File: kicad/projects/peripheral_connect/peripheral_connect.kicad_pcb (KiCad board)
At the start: 2 copper layers, 203.2 x 97.8 mm, 6 parts, among them J1 peripheral_addr_bus_connector, J2 peripheral_aux_connector, J3 peripheral_membank_connector

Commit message: Rough layout of peripheral connect PCB.
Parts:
- added C1: C, Capacitor_THT:C_Disc_D5.0mm_W2.5mm_P5.00mm, F.Cu at (90.9, 89.4)
- added C2: C, Capacitor_THT:C_Disc_D5.0mm_W2.5mm_P5.00mm, F.Cu at (89.7, 116.6)
- added C3: C, Capacitor_THT:C_Disc_D5.0mm_W2.5mm_P5.00mm, F.Cu at (133.1, 116.3)
- added C4: C, Capacitor_THT:C_Disc_D5.0mm_W2.5mm_P5.00mm, F.Cu at (98.6, 118.1)
- added C5: C, Capacitor_THT:C_Disc_D5.0mm_W2.5mm_P5.00mm, F.Cu at (200.7, 78.7)
- added C6: C, Capacitor_THT:C_Disc_D5.0mm_W2.5mm_P5.00mm, F.Cu at (155.8, 77.7)
- added C7: C, Capacitor_THT:C_Disc_D5.0mm_W2.5mm_P5.00mm, F.Cu at (102.1, 84.3)
- added C8: C, Capacitor_THT:C_Disc_D5.0mm_W2.5mm_P5.00mm, F.Cu at (54.9, 82.3)
- added D1: LED, sixteen-bit-computer:LED_D5.0mm_Horizontal_O3.81mm_Z3.0mm, F.Cu at (251.5, 63.5)
- added D10: LED, sixteen-bit-computer:LED_D5.0mm_Horizontal_O3.81mm_Z3.0mm, F.Cu at (196.6, 63.5)
- added D11: LED, sixteen-bit-computer:LED_D5.0mm_Horizontal_O3.81mm_Z3.0mm, F.Cu at (190.5, 63.5)
- added D12: LED, sixteen-bit-computer:LED_D5.0mm_Horizontal_O3.81mm_Z3.0mm, F.Cu at (184.4, 63.5)
- added D13: LED, sixteen-bit-computer:LED_D5.0mm_Horizontal_O3.81mm_Z3.0mm, F.Cu at (178.3, 63.5)
- added D14: LED, sixteen-bit-computer:LED_D5.0mm_Horizontal_O3.81mm_Z3.0mm, F.Cu at (172.2, 63.5)
- added D15: LED, sixteen-bit-computer:LED_D5.0mm_Horizontal_O3.81mm_Z3.0mm, F.Cu at (166.1, 63.5)
- added D16: LED, sixteen-bit-computer:LED_D5.0mm_Horizontal_O3.81mm_Z3.0mm, F.Cu at (160.0, 63.5)
- added D17: LED, sixteen-bit-computer:LED_D5.0mm_Horizontal_O3.81mm_Z3.0mm, F.Cu at (147.3, 63.5)
- added D18: LED, sixteen-bit-computer:LED_D5.0mm_Horizontal_O3.81mm_Z3.0mm, F.Cu at (141.2, 63.5)
- added D19: LED, sixteen-bit-computer:LED_D5.0mm_Horizontal_O3.81mm_Z3.0mm, F.Cu at (135.1, 63.5)
- added D2: LED, sixteen-bit-computer:LED_D5.0mm_Horizontal_O3.81mm_Z3.0mm, F.Cu at (245.4, 63.5)
- added D20: LED, sixteen-bit-computer:LED_D5.0mm_Horizontal_O3.81mm_Z3.0mm, F.Cu at (129.0, 63.5)
- added D21: LED, sixteen-bit-computer:LED_D5.0mm_Horizontal_O3.81mm_Z3.0mm, F.Cu at (122.9, 63.5)
- added D22: LED, sixteen-bit-computer:LED_D5.0mm_Horizontal_O3.81mm_Z3.0mm, F.Cu at (116.8, 63.5)
- added D23: LED, sixteen-bit-computer:LED_D5.0mm_Horizontal_O3.81mm_Z3.0mm, F.Cu at (110.7, 63.5)
- added D24: LED, sixteen-bit-computer:LED_D5.0mm_Horizontal_O3.81mm_Z3.0mm, F.Cu at (104.6, 63.5)
- added D25: LED, sixteen-bit-computer:LED_D5.0mm_Horizontal_O3.81mm_Z3.0mm, F.Cu at (98.6, 63.5)
- added D26: LED, sixteen-bit-computer:LED_D5.0mm_Horizontal_O3.81mm_Z3.0mm, F.Cu at (92.5, 63.5)
- added D27: LED, sixteen-bit-computer:LED_D5.0mm_Horizontal_O3.81mm_Z3.0mm, F.Cu at (86.4, 63.5)
- added D28: LED, sixteen-bit-computer:LED_D5.0mm_Horizontal_O3.81mm_Z3.0mm, F.Cu at (80.3, 63.5)
- added D29: LED, sixteen-bit-computer:LED_D5.0mm_Horizontal_O3.81mm_Z3.0mm, F.Cu at (74.2, 63.5)
- added D3: LED, sixteen-bit-computer:LED_D5.0mm_Horizontal_O3.81mm_Z3.0mm, F.Cu at (239.3, 63.5)
- added D30: LED, sixteen-bit-computer:LED_D5.0mm_Horizontal_O3.81mm_Z3.0mm, F.Cu at (68.1, 63.5)
- added D31: LED, sixteen-bit-computer:LED_D5.0mm_Horizontal_O3.81mm_Z3.0mm, F.Cu at (62.0, 63.5)
- added D32: LED, sixteen-bit-computer:LED_D5.0mm_Horizontal_O3.81mm_Z3.0mm, F.Cu at (55.9, 63.5)
- added D4: LED, sixteen-bit-computer:LED_D5.0mm_Horizontal_O3.81mm_Z3.0mm, F.Cu at (233.2, 63.5)
- added D5: LED, sixteen-bit-computer:LED_D5.0mm_Horizontal_O3.81mm_Z3.0mm, F.Cu at (227.1, 63.5)
- added D6: LED, sixteen-bit-computer:LED_D5.0mm_Horizontal_O3.81mm_Z3.0mm, F.Cu at (221.0, 63.5)
- added D7: LED, sixteen-bit-computer:LED_D5.0mm_Horizontal_O3.81mm_Z3.0mm, F.Cu at (214.9, 63.5)
- added D8: LED, sixteen-bit-computer:LED_D5.0mm_Horizontal_O3.81mm_Z3.0mm, F.Cu at (208.8, 63.5)
- added D9: LED, sixteen-bit-computer:LED_D5.0mm_Horizontal_O3.81mm_Z3.0mm, F.Cu at (202.7, 63.5)
- added J6: Conn_02x16_Odd_Even, Connector_PinHeader_2.54mm:PinHeader_2x16_P2.54mm_Vertical, F.Cu at (61.0, 91.7)
- added J7: ADDR, Connector_PinHeader_2.54mm:PinHeader_2x17_P2.54mm_Vertical, F.Cu at (203.2, 102.9)
- added J8: DATA, Connector_PinHeader_2.54mm:PinHeader_2x17_P2.54mm_Vertical, F.Cu at (243.8, 121.9)
- added RN1: R_Network08_US, Resistor_THT:R_Array_SIP9, F.Cu at (216.9, 70.6)
- added RN2: R_Network08_US, Resistor_THT:R_Array_SIP9, F.Cu at (170.2, 69.8)
- added RN3: R_Network08_US, Resistor_THT:R_Array_SIP9, F.Cu at (115.3, 69.6)
- added RN4: R_Network08_US, Resistor_THT:R_Array_SIP9, F.Cu at (66.8, 70.1)
- added U1: 74HC138, Package_DIP:DIP-16_W7.62mm_Socket, F.Cu at (150.6, 120.9)
- added U2: 74HC138, Package_DIP:DIP-16_W7.62mm_Socket, F.Cu at (116.1, 122.4)
- added U3: 74HC238, Package_DIP:DIP-16_W7.62mm_Socket, F.Cu at (77.5, 116.8)
- added U4: 74HC245, Package_DIP:DIP-20_W7.62mm_Socket, F.Cu at (210.3, 84.3)
- added U5: 74HC238, Package_DIP:DIP-16_W7.62mm_Socket, F.Cu at (77.5, 89.9)
- added U6: 74HC245, Package_DIP:DIP-20_W7.62mm_Socket, F.Cu at (164.8, 83.3)
- added U7: 74HC245, Package_DIP:DIP-20_W7.62mm_Socket, F.Cu at (109.7, 81.8)
- added U8: 74HC245, Package_DIP:DIP-20_W7.62mm_Socket, F.Cu at (62.2, 83.1)
- moved C99 33.2 mm to (29.3, 145.5)
- moved C97 27.7 mm to (37.7, 42.7)
- moved C98 26.8 mm to (266.0, 46.0)
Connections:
- J2 pad 10: unconnected-(J2-RFM-Pad10) -> /RFM
- J2 pad 12: unconnected-(J2-WTM-Pad12) -> /WTM
- J2 pad 14: unconnected-(J2-RST-Pad14) -> /RESET
- J2 pad 6: unconnected-(J2-DCLK-Pad6) -> /DATA_CLK
- J2 pad 8: unconnected-(J2-CCLK-Pad8) -> /CTL_CLK

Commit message: Un invert counter addressed. Almost done on peripheral connect PCB.
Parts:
- added J4: Conn_01x03_Pin, Connector_PinHeader_2.54mm:PinHeader_1x03_P2.54mm_Horizontal, F.Cu at (241.3, 88.9)
- added R1: 10K, Resistor_THT:R_Axial_DIN0207_L6.3mm_D2.5mm_P10.16mm_Horizontal, F.Cu at (247.1, 83.8)
- RN1, RN2: value R_Network08_US -> 10K
- RN3, RN4: value R_Network08_US -> 1K
- moved C98 81.1 mm to (194.6, 84.4), turned to -90 degrees
- moved C97 70.6 mm to (95.2, 83.6)
- moved C99 28.2 mm to (56.9, 139.7), turned to 90 degrees
- moved C4 27.4 mm to (124.5, 127.0), turned to 90 degrees
- moved C3 26.6 mm to (157.5, 127.0), turned to 90 degrees
- moved C5 10.5 mm to (210.8, 76.2), turned to -90 degrees
- moved C7 8.37 mm to (104.1, 76.2), turned to -90 degrees
- moved J7 6.35 mm to (203.2, 96.5)
- moved U4 5.61 mm to (215.9, 83.8)
- moved C6 5.48 mm to (160.0, 81.2), turned to 90 degrees
- moved U2 3.15 mm to (116.8, 119.4)
- moved C1 2.87 mm to (88.9, 91.4)
- moved RN1 2.84 mm to (219.7, 71.1)
- moved RN3 2.75 mm to (113.0, 71.1)
- moved RN4 2.27 mm to (64.8, 71.1)
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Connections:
- RN1 pad 1: unconnected-(RN1-common-Pad1) -> VCC
- RN1 pad 2: Net-(D8-K) -> Net-(D8-A)
- RN1 pad 3: Net-(D7-K) -> Net-(D7-A)
- RN1 pad 4: Net-(D6-K) -> Net-(D6-A)
- RN1 pad 5: Net-(D5-K) -> Net-(D5-A)
- RN1 pad 6: Net-(D4-K) -> Net-(D4-A)
- RN1 pad 7: Net-(D3-K) -> Net-(D3-A)
- RN1 pad 8: Net-(D2-K) -> Net-(D2-A)
- RN1 pad 9: Net-(D1-K) -> Net-(D1-A)
- RN2 pad 1: unconnected-(RN2-common-Pad1) -> VCC
- RN2 pad 2: Net-(D16-K) -> Net-(D16-A)
- RN2 pad 3: Net-(D15-K) -> Net-(D15-A)
- RN2 pad 4: Net-(D14-K) -> Net-(D14-A)
- RN2 pad 5: Net-(D13-K) -> Net-(D13-A)
- RN2 pad 6: Net-(D12-K) -> Net-(D12-A)
- RN2 pad 7: Net-(D11-K) -> Net-(D11-A)
- RN2 pad 8: Net-(D10-K) -> Net-(D10-A)
- RN2 pad 9: Net-(D9-K) -> Net-(D9-A)
- RN3 pad 1: unconnected-(RN3-common-Pad1) -> GND
- RN4 pad 1: unconnected-(RN4-common-Pad1) -> GND
- U4 pad 11: Net-(D1-A) -> Net-(D1-K)
- U4 pad 12: Net-(D2-A) -> Net-(D2-K)
- U4 pad 13: Net-(D3-A) -> Net-(D3-K)
- U4 pad 14: Net-(D4-A) -> Net-(D4-K)
- U4 pad 15: Net-(D5-A) -> Net-(D5-K)
- U4 pad 16: Net-(D6-A) -> Net-(D6-K)
- U4 pad 17: Net-(D7-A) -> Net-(D7-K)
- U4 pad 18: Net-(D8-A) -> Net-(D8-K)
- U4 pad 19: unconnected-(U4-~{OE}-Pad19) -> /~{LED ENABLE}
- U6 pad 11: Net-(D9-A) -> Net-(D9-K)
- U6 pad 12: Net-(D10-A) -> Net-(D10-K)
- U6 pad 13: Net-(D11-A) -> Net-(D11-K)
- U6 pad 14: Net-(D12-A) -> Net-(D12-K)
- U6 pad 15: Net-(D13-A) -> Net-(D13-K)
- U6 pad 16: Net-(D14-A) -> Net-(D14-K)
- U6 pad 17: Net-(D15-A) -> Net-(D15-K)
- U6 pad 18: Net-(D16-A) -> Net-(D16-K)
- U6 pad 19: unconnected-(U6-~{OE}-Pad19) -> /~{LED ENABLE}
- U7 pad 19: unconnected-(U7-~{OE}-Pad19) -> /~{LED ENABLE}
- U8 pad 19: unconnected-(U8-~{OE}-Pad19) -> /~{LED ENABLE}
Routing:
- net VCC: track 0.00 -> 498.2 mm, vias 0 -> 12
- net /ADDR_BUS_00: track 0.00 -> 207.2 mm, vias 0 -> 6
- net /ADDR_BUS_01: track 0.00 -> 203.3 mm, vias 0 -> 6
- net /ADDR_BUS_03: track 0.00 -> 202.5 mm, vias 0 -> 5
- net /~{LED ENABLE}: track 0.00 -> 201.9 mm, vias 0 -> 5
- net /ADDR_BUS_02: track 0.00 -> 200.4 mm, vias 0 -> 6
- net /BANK_BUS_15: track 0.00 -> 167.3 mm, vias 0 -> 5
- net /BANK_BUS_07: track 0.00 -> 154.1 mm, vias 0 -> 4
- net /BANK_BUS_06: track 0.00 -> 145.4 mm, vias 0 -> 2
- net /BANK_BUS_05: track 0.00 -> 144.7 mm, vias 0 -> 2
- net /BANK_BUS_04: track 0.00 -> 143.9 mm, vias 0 -> 2
- net /BANK_BUS_03: track 0.00 -> 143.0 mm, vias 0 -> 2
- net /BANK_BUS_02: track 0.00 -> 142.2 mm, vias 0 -> 2
- net /BANK_BUS_01: track 0.00 -> 141.0 mm, vias 0 -> 2
- net /BANK_BUS_00: track 0.00 -> 139.9 mm, vias 0 -> 2
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
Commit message: Tech chekcs on Peripheral connect
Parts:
- C97, C98, C99: value C_Polarized -> 33uF
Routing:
- net /BANK_BUS_07: track 154.1 -> 146.5 mm, vias 4 -> 2
- net /BANK_BUS_00: track 139.9 -> 143.0 mm
- net /BANK_BUS_01: track 141.0 -> 143.7 mm
- net /BANK_BUS_02: track 142.2 -> 144.4 mm
- net /BANK_BUS_03: track 143.0 -> 144.8 mm
- net /BANK_BUS_04: track 143.9 -> 145.1 mm
- net /ADDR_BUS_13: track 120.0 -> 118.9 mm
- net /BANK_BUS_05: track 144.7 -> 145.6 mm
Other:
- board text added: "0"
- board text added: "1"
- board text added: "10"
- board text added: "11"
- board text added: "12"
- board text added: "13"
- board text added: "14"
- board text added: "15"
- board text added: "2"
- board text added: "3"
- board text added: "4"
- board text added: "5"
- board text added: "6"
- board text added: "7"
- board text added: "8"
- board text added: "9"
- board text added: "ADDRESS BUS"
- board text added: "BUS CONNECT DEVICE AND BANK DECODE"
- board text added: "Bank"
- board text added: "DATA BUS"
- board text added: "Device"
- board text added: "Device Addressed"
- board text added: "GND"
- board text added: "JLCJLCJLCJLC"
- board text added: "LED ~{OE}"
- board text added: "SIGNAL"
- board text added: "VCC"
- board text added: "X"
- board text added: "v1.0"

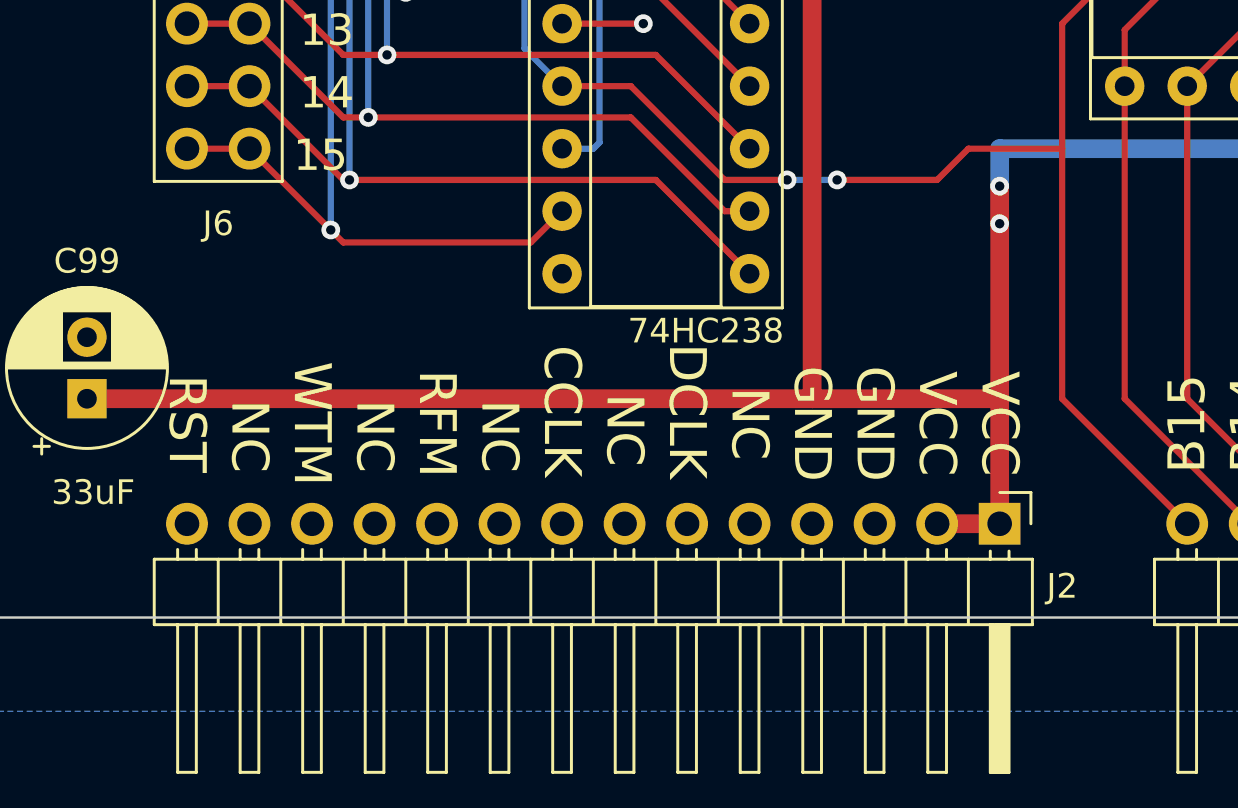
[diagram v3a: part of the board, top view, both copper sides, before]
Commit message: Peripheral connect updated to one wire rfm wtm.
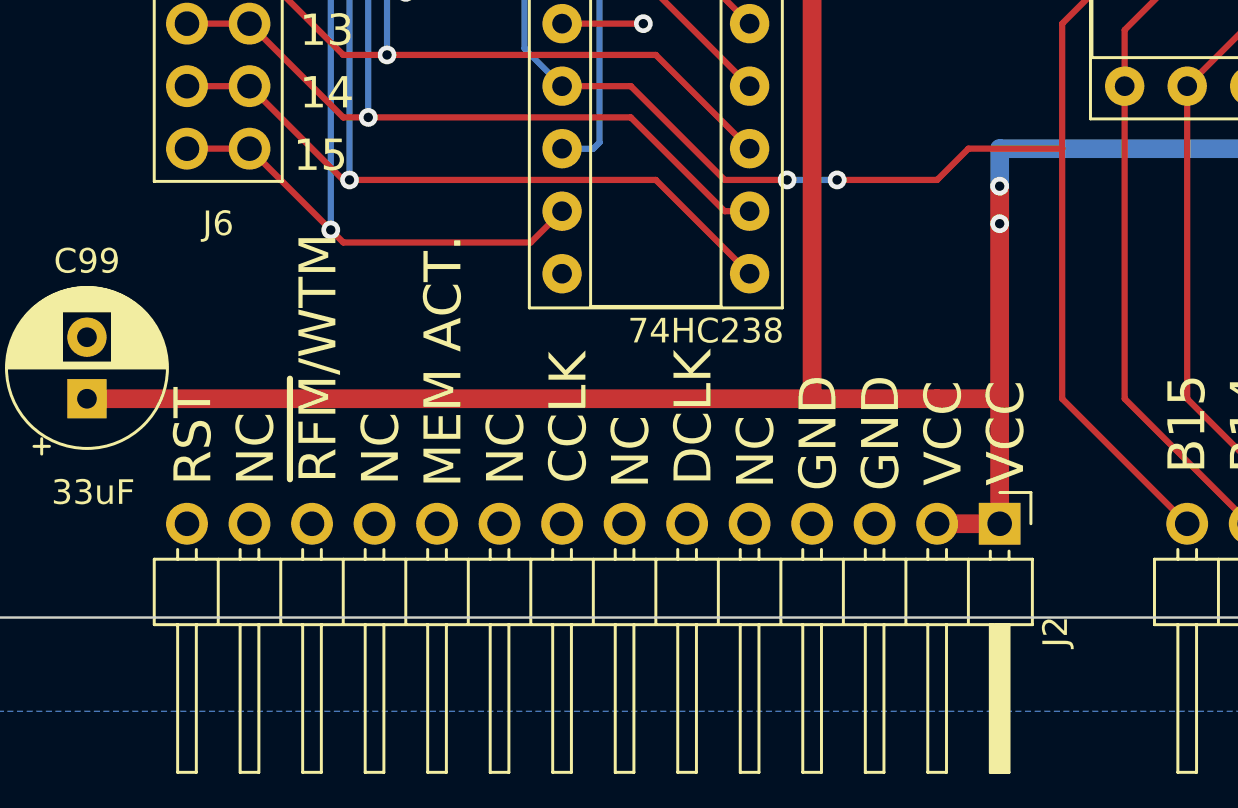
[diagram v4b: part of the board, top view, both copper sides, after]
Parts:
- turned J2 to 0 degrees
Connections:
- net /RFM renamed /MEM_ACTIVE
- net /WTM renamed /RFM_WTM

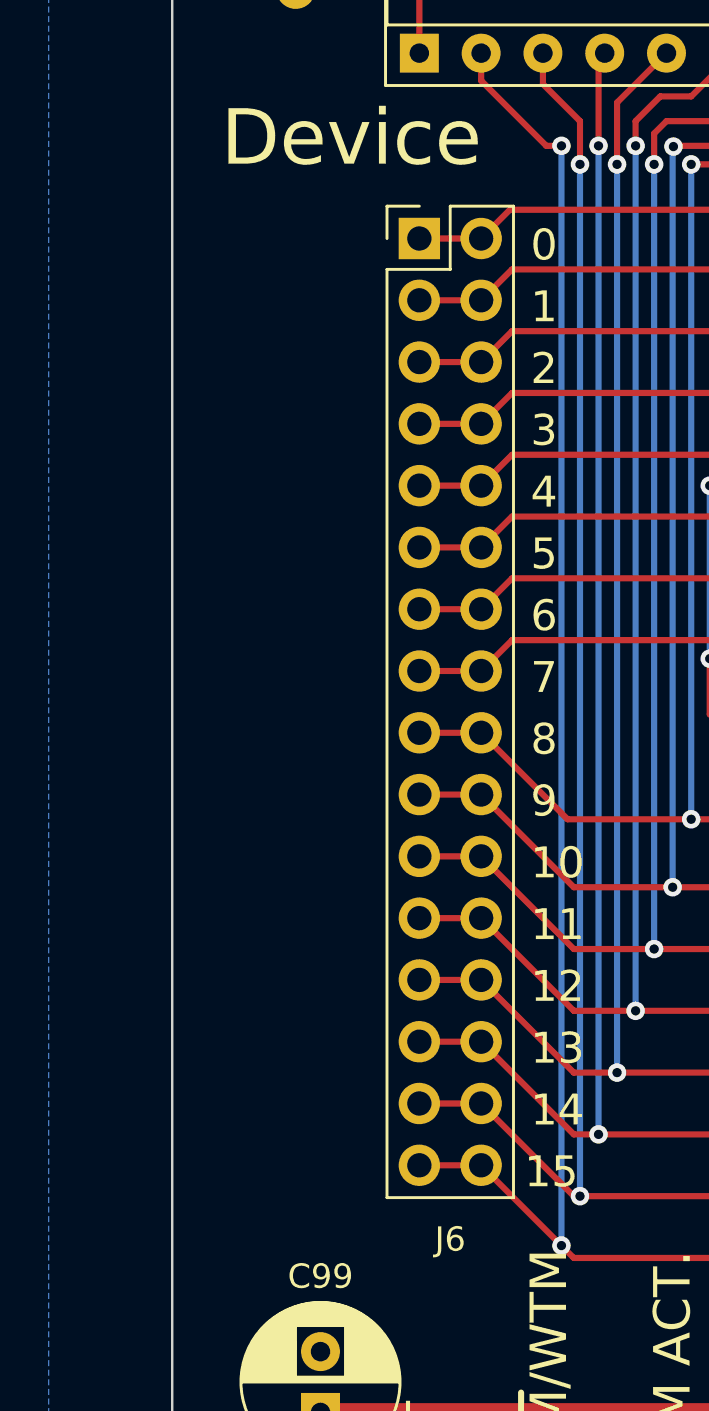
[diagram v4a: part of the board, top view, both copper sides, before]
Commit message: Add double row pin socket to peripheral connect.
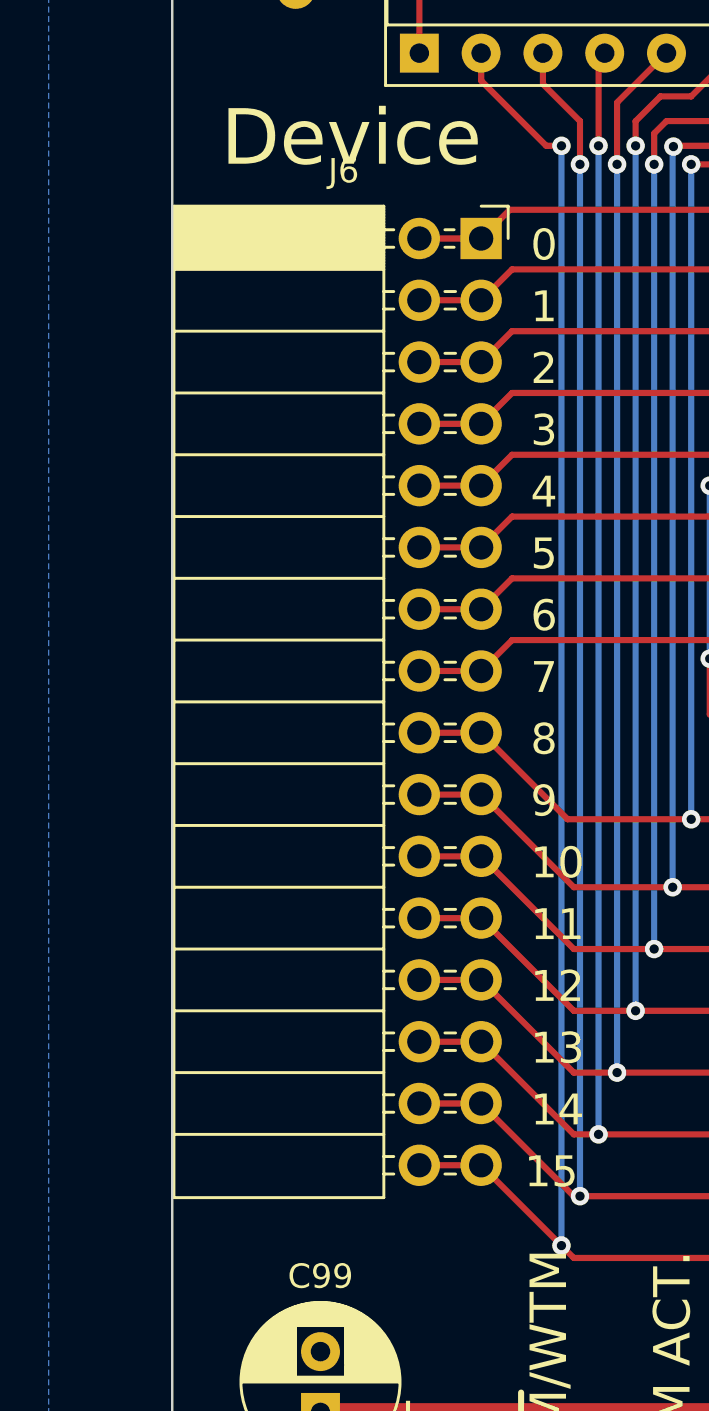
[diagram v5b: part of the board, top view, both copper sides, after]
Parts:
- J6: footprint Connector_PinHeader_2.54mm:PinHeader_2x16_P2.54mm_Vertical -> Connector_PinSocket_2.54mm:PinSocket_2x16_P2.54mm_Horizontal
- moved J6 2.54 mm to (63.5, 91.4)
